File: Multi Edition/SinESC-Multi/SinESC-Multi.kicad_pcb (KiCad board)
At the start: 4 copper layers, 30 x 15 mm, 84 parts, among them J1 Pad_3x2mm, J2 Pad_3x2mm, J3 Pad_3x2mm, J4 Pad_3x2mm, J5 Pad_3x2mm, J6 Pad_1.5mm_Square, Q1 BSC010N04LSI, Q2 BSC010N04LSI, Q3 BSC010N04LSI, Q4 BSC010N04LSI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

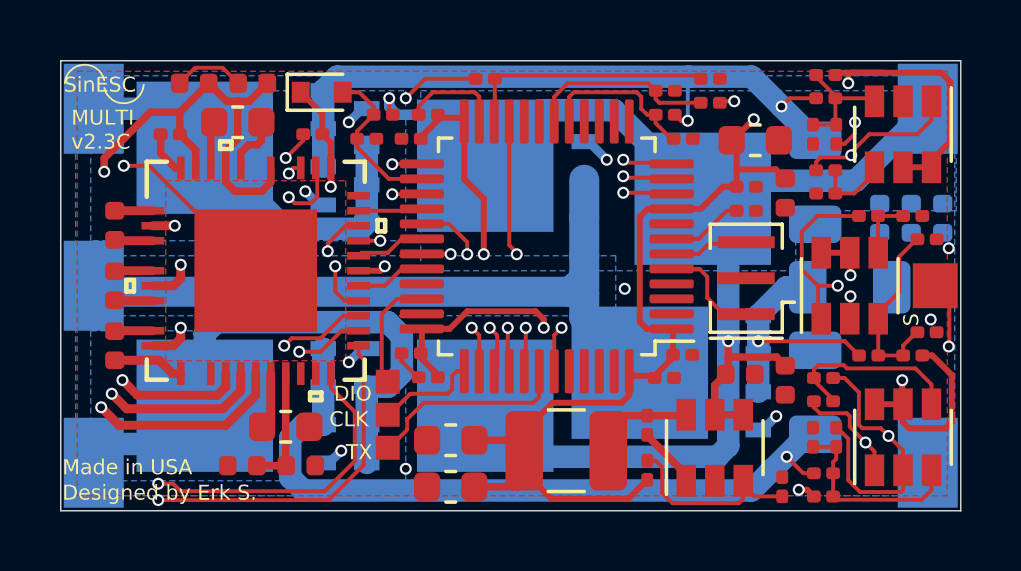
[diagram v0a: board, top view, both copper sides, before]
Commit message: Change via drill diameter to 0.2mm from 0.254mm. This allows the design to take full advantage of PCBWay's capabilities, while it remains compatible with OSH Park's minimum design rules as well (as they simply increase the via drill diameter slightly)
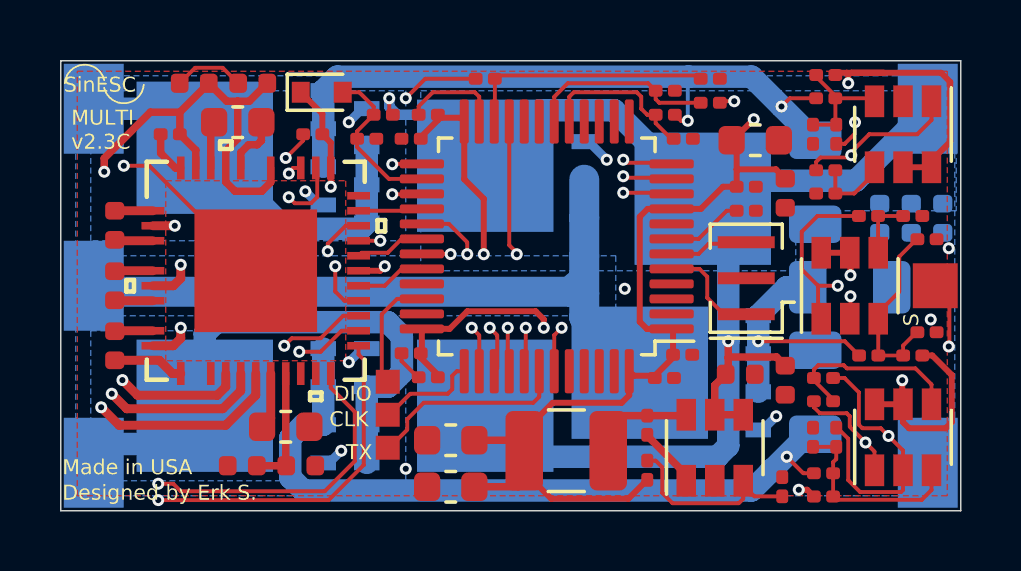
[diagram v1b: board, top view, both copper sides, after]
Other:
- net class +3V3: via_drill 0.254 -> 0.2
- net class Buck Converter: via_drill 0.254 -> 0.2
- net class Default: via_drill 0.254 -> 0.2
- net class Gates: via_drill 0.254 -> 0.2
- net class High-Current: via_drill 0.254 -> 0.2
- rule via_min_drill: 0.254 -> 0.2
